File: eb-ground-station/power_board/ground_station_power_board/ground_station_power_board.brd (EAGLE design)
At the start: 142 x 81.8 mm, 52 parts, among them J1 CONN_20X2SHROUDED, U1 ADS1115IDGSTDGS10-M, U2 MCP23017T-E/SOSOIC28-W_MC-M, U3 MICROCHIP-TC427-MOSFET-DRIVER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, U4 MICROCHIP-TC427-MOSFET-DRIVER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, U5 MICROCHIP-TC427-MOSFET-DRIVER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, U6 NCV1117ST33T3G, U7 EXB-A10P391JC_ARRAY_EXBA-M, U8 EXB-A10P391JC_ARRAY_EXBA-M, U9 EXB-A10P391JC_ARRAY_EXBA-M

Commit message: Power board is mostly wrapped up
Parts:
- removed J2, J3: (no value), SparkFun-Connectors:1X03_LONGPADS
- removed R10, R11, R12, R4, R5, R6, R7, R8, R9: (no value), SparkFun-Resistors:0603
- removed U5: MICROCHIP-TC427-MOSFET-DRIVERSOIC8, GROUND-STATION-POWER-BOARD:SOIC8
- removed U6: NCV1117ST33T3G, NCV1117ST33T3G:SOT230P700X180-4N
- added D1, D10, D11, D12, D13, D14, D15, D16, D17, D2, D3, D4, D5, D6, D7, D8, D9: (no value), SparkFun-LED:LED-0603
- added J4: (no value), SparkFun-Connectors:1X06_LONGPADS
- added J5: (no value), SparkFun-Connectors:1X04_LONGPADS
- added U$19, U$20, U$21, U$25, U$26, U$27, U$28: RES-ARRAY-742C083, GROUND-STATION-POWER-BOARD:RES-ARRAY-742C083
- added U$22, U$23, U$24: TC4427-FET-GATE-DRVR, GROUND-STATION-POWER-BOARD:TSSOP-8
- R3: value 220 -> 800
- U$7: value 1714971-PHONEIX-CONTACT-TERMINAL-BLOCK -> 1714955-PHONEIX-CONTACT-TERMINAL-BLOCK; device GROUND-STATION-POWER-BOARD:1714971-PHONEIX-CONTACT-TERMINAL-BLOCK -> GROUND-STATION-POWER-BOARD:1714955-PHONEIX-CONTACT-TERMINAL-BLOCK
- U2: value MCP23017T-E/SOSOIC28-W_MC-M -> MCP23017T-E/SOQFN; device GROUND-STATION-POWER-BOARD:SOIC28-W_MC-M -> GROUND-STATION-POWER-BOARD:QFN28_6X6MC-M
- U3: value MICROCHIP-TC427-MOSFET-DRIVERSOIC8 -> MIC5239-3.3YMMMSOP-8_MM-M; device GROUND-STATION-POWER-BOARD:SOIC8 -> GROUND-STATION-POWER-BOARD:MSOP-8_MM-M
- U4: value MICROCHIP-TC427-MOSFET-DRIVERSOIC8 -> MCP9808T-E/MCDFN8_2X3MC-M; device GROUND-STATION-POWER-BOARD:SOIC8 -> GROUND-STATION-POWER-BOARD:DFN8_2X3MC-M
- moved R3 131.5 mm to (116.2, 27.4)
- moved U4 87.6 mm to (12.0, 70.0), turned to 0 degrees
- moved U$9 82.6 mm to (41.5, 25.2), turned to 0 degrees
- moved U9 81.5 mm to (60.6, 25.9), turned to 180 degrees
- moved C5 80.9 mm to (15.0, 34.5), turned to 180 degrees
- moved C7 75.6 mm to (31.1, 42.4), turned to 0 degrees
- moved C9 71.9 mm to (45.8, 36.7), turned to 270 degrees
- moved C6 70.5 mm to (30.9, 37.9), turned to 270 degrees
- moved R2 66.5 mm to (15.0, 38.5)
- moved C10 63.3 mm to (59.8, 36.7), turned to 270 degrees
- moved C8 60.5 mm to (52.8, 36.7), turned to 270 degrees
- moved R1 59.9 mm to (15.0, 36.5)
- moved U$17 59.1 mm to (48.5, 25.2)
- moved C3 56.3 mm to (32.8, 38.0), turned to 270 degrees
- moved C4 55.2 mm to (39.0, 38.0), turned to 270 degrees
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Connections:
- removed net N$10: R12.1
- removed net N$21: R11.2, U$8.2
- removed net N$23: R12.2, U$8.5
- removed net N$25: R6.2, U$17.2
- removed net N$30: R5.2, U$18.2
- removed net N$31: R8.2, U$15.5
- removed net N$32: R3.2, U$18.5
- removed net N$33: R9.2, U$9.2
- removed net N$34: R10.2, U$9.5
- removed net N$5: R7.1
- removed net N$6: R8.1
- removed net N$7: R9.1
- removed net N$8: R10.1
- new net ADC1: U$5.3, U1.7
- new net ADC2: U$5.1, U1.6
- new net ADC3: U$6.3, U1.5
- new net ADC4: U$6.1, U1.4
- new net G1: U$21.6, U$8.5
- new net G10: U$17.2, U$20.4
- new net G2: U$21.8, U$8.2
- new net G3: U$19.2, U$9.5
- new net G4: U$19.4, U$9.2
- new net G5: U$15.5, U$19.6
- new net G6: U$15.2, U$19.8
- new net G7: U$18.5, U$20.6
- new net G8: U$18.2, U$20.8
- new net G9: U$17.5, U$20.2
- new net HIGH_OUT_1: U$24.7, U$3.4
- new net HIGH_OUT_2: U$24.5, U$3.2
- new net HIGH_OUT_3: U$1.4, U$23.7
- new net HIGH_OUT_4: U$1.2, U$23.5
- new net HIGH_OUT_5: U$2.4, U$22.7
- new net HIGH_OUT_6: U$2.2, U$22.5
- new net LOW_OUT_1: U$18.3, U$4.3
- new net LOW_OUT_2: U$18.6, U$4.4
- new net LOW_OUT_3: U$17.3, U$4.2
- new net LOW_OUT_4: U$17.6, U$4.1
- new net N$14: D6.A, U$26.8
- new net N$15: D7.A, U$26.6
- new net N$16: D8.A, U$26.4
- new net N$17: D9.A, U$26.2
- new net N$27: D11.A, U$27.6
- new net N$28: D12.A, U$27.4
- new net N$38: D14.A, U$28.8
- new net N$39: D15.A, U$28.6
- new net N$40: D16.A, U$28.4
- new net N$41: D17.A, U$28.2
- new net RX: J4.4
- new net TX: J4.5
- net 12V: now also D5.A, U$22.6, U$23.6, U$24.6, U3.1, U3.3; no longer U3.6, U4.6, U5.6, U6.3
- net 3.3V: now also J4.3, J5.3, U2.5, U3.4, U4.8; no longer U2.9, U6.2, U6.4
- net GND: now also D1.C, D10.C, D11.C, D12.C, D13.C, D14.C, D15.C, D16.C, D17.C, D2.C, D3.C, D4.C, D6.C, D7.C, D8.C, D9.C, J4.1, J5.4, R3.2, U$22.3, U$23.3, U$24.3, U$5.2, U$5.4, U$6.2, U$6.4, U1.1, U2.11, U2.12, U2.13, U2.14, U2.29, U2.6, U3.5, U3.6, U3.7, U3.8, U4.4, U4.5, U4.6, U4.7, U4.9; no longer U2.10, U2.18, U3.3, U4.3, U5.3, U6.1
- net N$1: now also D1.A, U$25.8; no longer R3.1
- net N$2: now also D2.A, U$25.6; no longer R5.1
- net N$26: now also D10.A, U$27.8; no longer R4.2, U$17.5
- net N$29: now also D13.A, U$27.2; no longer R7.2, U$15.2
- net N$3: now also D3.A, U$25.4; no longer R4.1
- net N$4: now also D4.A, U$25.2; no longer R6.1
- net N$9: now also D5.C, R3.1; no longer R11.1
- net OUT1: now also U$24.4, U$26.5, U2.27, U8.2; no longer U2.21, U8.6
- net OUT10: now also U$20.1, U$27.5, U2.23; no longer U2.2
- net OUT11: now also U$19.3, U$28.7, U2.20, U7.8; no longer U2.3, U7.7
- net OUT12: now also U$19.7, U$27.3, U2.22, U7.7; no longer U2.4, U7.3
- net OUT13: now also U$19.5, U$27.1, U2.21, U7.3; no longer U2.5, U7.8
- net OUT14: now also U$19.1, U$28.5, U2.19; no longer U2.6
- net OUT15: now also U$21.7, U$28.3, U2.18; no longer U2.7
- net OUT16: now also U$21.5, U$28.1, U2.17; no longer U2.8
- net OUT2: now also U$24.2, U$26.7, U2.28, U8.8; no longer U2.22, U8.4
- net OUT3: now also U$23.4, U$25.5, U2.3, U8.4; no longer U2.23, U8.7
- net OUT4: now also U$23.2, U$25.7, U2.4, U8.6; no longer U2.24, U8.3
- net OUT5: now also U$22.4, U$25.1, U2.1, U8.3; no longer U2.25, U8.8
- net OUT6: now also U$22.2, U$25.3, U2.2, U8.7; no longer U2.26, U8.2
- net OUT7: now also U$20.7, U$26.3, U2.26; no longer U2.27
- net OUT8: now also U$20.5, U$26.1, U2.25; no longer U2.28
- net OUT9: now also U$20.3, U$27.7, U2.24; no longer U2.1
- net PWR_FET_G1: now also U$10.G, U9.8; no longer U$16.G, U9.1
- net PWR_FET_G2: now also U$16.G, U9.2; no longer U$10.G, U9.9
- net PWR_FET_G3: now also U$12.G, U9.7; no longer U$11.G, U9.2
- net PWR_FET_G4: now also U$11.G, U9.3; no longer U$12.G, U9.8
- net PWR_FET_G5: now also U$14.G, U9.6; no longer U$13.G, U9.3
- net PWR_FET_G6: now also U$13.G, U9.4; no longer U$14.G, U9.7
- net SCL: now also J5.1, U2.8, U4.2; no longer U2.12
- net SDA: now also J5.2, U2.9, U4.1; no longer U2.13
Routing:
- net PWR_FET_G2: track 0.00 -> 81.1 mm, vias 0 -> 2
- net N$40: track 0.00 -> 75.3 mm
- net SDA: track 0.00 -> 73.6 mm, vias 0 -> 3
- net N$15: track 0.00 -> 70.6 mm
- net N$41: track 0.00 -> 69.4 mm
- net SCL: track 0.00 -> 68.8 mm
- net PWR_FET_G1: track 0.00 -> 68.5 mm, vias 0 -> 2
- net 3.3V: track 0.00 -> 68.0 mm
- net HIGH_OUT_1: track 0.00 -> 67.9 mm, vias 0 -> 1
- net OUT1: track 0.00 -> 67.0 mm, vias 0 -> 2
- net N$14: track 0.00 -> 65.6 mm
- net N$38: track 0.00 -> 65.3 mm
- net HIGH_OUT_2: track 0.00 -> 65.1 mm, vias 0 -> 1
- net PWR_FET_G4: track 0.00 -> 64.5 mm, vias 0 -> 2
- net OUT2: track 0.00 -> 64.1 mm, vias 0 -> 2
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- added copper zone on layer 1, net 12V
- added copper zone on layer 16, net 12V
- added copper zone on layer 1, net GND
- added copper zone on layer 16, net GND
- added copper zone on layer 1, net PWR_P_FET_1
- added copper zone on layer 1, net PWR_P_FET_2
- added copper zone on layer 1, net PWR_P_FET_3
- added copper zone on layer 1, net PWR_P_FET_4
- added copper zone on layer 1, net PWR_P_FET_5
- added copper zone on layer 1, net PWR_P_FET_6
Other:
- board size 142 x 81.8 mm -> 125 x 78 mm
- board text added: "1"
- board text added: "12V"
- board text added: "2"
- board text added: "3"
- board text added: "4"
- board text added: "5"
- board text added: "6"
- board text added: "A0"
- board text added: "A1"
- board text added: "A2"
- board text added: "A3"
- board text added: "A4"
- board text added: "A5"
- board text added: "A6"
- board text added: "A7"
- board text added: "ADC-IN"
- board text added: "B0"
- board text added: "B1"
- board text added: "B2"
- board text added: "B3"
- board text added: "B4"
- board text added: "B5"
- board text added: "B6"
- board text added: "B7"
- board text added: "G"
- board text added: "GND"
- board text added: "GROUND"
- board text added: "HIGH-SIDE"
- board text added: "HIGH-SIDE-HIGH-POWER"
- board text added: "LOW-SIDE"

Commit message: some final changes
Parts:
- removed U$10, U$11, U$12, U$13, U$14, U$16: SQJ459EP_MOSFET_P_CHAN, GROUND-STATION-POWER-BOARD:POWERPAK_S0-8L
- removed U$15, U$17, U$18, U$8, U$9: DMN61D8LVT-DUAL-N-CHANNEL-MOSFET, GROUND-STATION-POWER-BOARD:TSOT26
- removed U$19, U$20, U$21, U$25, U$26, U$27, U$28: RES-ARRAY-742C083, GROUND-STATION-POWER-BOARD:RES-ARRAY-742C083
- removed U$22, U$23, U$24: TC4427-FET-GATE-DRVR, GROUND-STATION-POWER-BOARD:TSSOP-8
- removed U7, U8, U9: EXB-A10P391JC_ARRAY_EXBA-M, temp-lib:C_ARRAY_EXBA-M
- added E1, E2: (no value), oresat-rcl:.0805-B
- added Q1, Q2, Q3, Q4, Q5, Q6: SQJ459EP_MOSFET_P_CHAN, GROUND-STATION-POWER-BOARD:POWERPAK_S0-8L
- added Q15, Q17, Q18, Q8, Q9: DMN61D8LVT-DUAL-N-CHANNEL-MOSFET, GROUND-STATION-POWER-BOARD:TSOT26
- added Q22, Q23, Q24: TC4427-FET-GATE-DRVR, GROUND-STATION-POWER-BOARD:TSSOP-8
- added R10, R8, R9: EXB-A10P391JC_ARRAY_EXBA-M, temp-lib:C_ARRAY_EXBA-M
- added R11, R12, R13: 220, GROUND-STATION-POWER-BOARD:RES-ARRAY-742C083
- added R4, R5, R6, R7: 680, GROUND-STATION-POWER-BOARD:RES-ARRAY-742C083
- C10, C4, C8, C9: device SparkFun-Capacitors:1206 -> SparkFun-Capacitors:0805
- C2: value 100UF-CAP-EMVH630ARA101MKE0SCHEMI-KE0-M -> 100UF
- C3: value 4.7uF -> 10uF; device SparkFun-Capacitors:1206 -> SparkFun-Capacitors:0805
- R3: value 800 -> 806
- moved U4 118.5 mm to (113.0, 8.00), turned to 180 degrees
- moved J4 115.8 mm to (112.0, 69.0), turned to 270 degrees
- moved J1 115.0 mm to (120.0, 39.0), turned to 180 degrees
- moved U$7 110.2 mm to (16.3, 8.97), turned to 0 degrees
- moved D5 106.7 mm to (15.9, 62.1), turned to 0 degrees
- moved R3 105.5 mm to (15.9, 60.0), turned to 180 degrees
- moved D16 99.6 mm to (26.5, 68.0), turned to 180 degrees
- moved J5 99.4 mm to (102.5, 61.4)
- moved C2 98.7 mm to (15.8, 23.2), turned to 0 degrees
- moved C5 95.4 mm to (110.0, 43.5), turned to 0 degrees
- moved R1 95.1 mm to (110.0, 41.5), turned to 180 degrees
- moved R2 95.0 mm to (110.0, 39.5), turned to 180 degrees
- moved U2 93.6 mm to (108.3, 48.4), turned to 90 degrees
- moved C1 93.0 mm to (16.6, 31.5), turned to 0 degrees
- moved D17 91.7 mm to (31.5, 68.0), turned to 180 degrees
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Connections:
- removed net RX: J4.4
- removed net TX: J4.5
- new net AGND: C6.2, E2.2, U$5.2, U$5.4, U$6.2, U$6.4, U1.1, U1.2, U1.3
- new net N$5: C6.1, E1.1, U1.8
- net 12V: now also Q1.S1, Q1.S2, Q1.S3, Q2.S1, Q2.S2, Q2.S3, Q22.6, Q23.6, Q24.6, Q3.S1, Q3.S2, Q3.S3, Q4.S1, Q4.S2, Q4.S3, Q5.S1, Q5.S2, Q5.S3, Q6.S1, Q6.S2, Q6.S3, R10.10, R10.5; no longer U$10.S1, U$10.S2, U$10.S3, U$11.S1, U$11.S2, U$11.S3, U$12.S1, U$12.S2, U$12.S3, U$13.S1, U$13.S2, U$13.S3, U$14.S1, U$14.S2, U$14.S3, U$16.S1, U$16.S2, U$16.S3, U$22.6, U$23.6, U$24.6, U9.10, U9.5
- net 3.3V: now also E1.2; no longer C6.1, U1.8
- net G1: now also Q8.5, R11.6; no longer U$21.6, U$8.5
- net G10: now also Q17.2, R13.4; no longer U$17.2, U$20.4
- net G2: now also Q8.2, R11.8; no longer U$21.8, U$8.2
- net G3: now also Q9.5, R12.2; no longer U$19.2, U$9.5
- net G4: now also Q9.2, R12.4; no longer U$19.4, U$9.2
- net G5: now also Q15.5, R12.6; no longer U$15.5, U$19.6
- net G6: now also Q15.2, R12.8; no longer U$15.2, U$19.8
- net G7: now also Q18.5, R13.6; no longer U$18.5, U$20.6
- net G8: now also Q18.2, R13.8; no longer U$18.2, U$20.8
- net G9: now also Q17.5, R13.2; no longer U$17.5, U$20.2
- net GND: now also E2.1, Q15.1, Q15.4, Q17.1, Q17.4, Q18.1, Q18.4, Q22.3, Q23.3, Q24.3, Q8.1, Q8.4, Q9.1, Q9.4, R8.10, R8.5, R9.10, R9.5; no longer C6.2, U$15.1, U$15.4, U$17.1, U$17.4, U$18.1, U$18.4, U$22.3, U$23.3, U$24.3, U$5.2, U$5.4, U$6.2, U$6.4, U$8.1, U$8.4, U$9.1, U$9.4, U1.1, U1.3, U7.10, U7.5, U8.10, U8.5
- net HIGH_OUT_1: now also Q24.7; no longer U$24.7
- net HIGH_OUT_2: now also Q24.5; no longer U$24.5
- net HIGH_OUT_3: now also Q23.7; no longer U$23.7
- net HIGH_OUT_4: now also Q23.5; no longer U$23.5
- net HIGH_OUT_5: now also Q22.7; no longer U$22.7
- net HIGH_OUT_6: now also Q22.5; no longer U$22.5
- net LOW_OUT_1: now also Q18.3; no longer U$18.3
- net LOW_OUT_2: now also Q18.6; no longer U$18.6
- net LOW_OUT_3: now also Q17.3; no longer U$17.3
- net LOW_OUT_4: now also Q17.6; no longer U$17.6
- net N$1: now also R4.8; no longer U$25.8
- net N$14: now also R5.8; no longer U$26.8
- net N$15: now also R5.6; no longer U$26.6
- net N$16: now also R5.4; no longer U$26.4
- net N$17: now also R5.2; no longer U$26.2
- net N$2: now also R4.6; no longer U$25.6
- net N$26: now also R6.8; no longer U$27.8
- net N$27: now also R6.6; no longer U$27.6
- net N$28: now also R6.4; no longer U$27.4
- net N$29: now also R6.2; no longer U$27.2
- net N$3: now also R4.4; no longer U$25.4
- net N$38: now also R7.8; no longer U$28.8
- net N$39: now also R7.6; no longer U$28.6
- net N$4: now also R4.2; no longer U$25.2
- net N$40: now also R7.4; no longer U$28.4
- net N$41: now also R7.2; no longer U$28.2
- net OUT1: now also Q24.4, R5.5, R8.2; no longer U$24.4, U$26.5, U8.2
- net OUT10: now also R13.1, R6.5, R9.4; no longer U$20.1, U$27.5, U7.4
- net OUT11: now also R12.3, R7.7, R9.8; no longer U$19.3, U$28.7, U7.8
- net OUT12: now also R12.7, R6.3, R9.7; no longer U$19.7, U$27.3, U7.7
- net OUT13: now also R12.5, R6.1, R9.3; no longer U$19.5, U$27.1, U7.3
- net OUT14: now also R12.1, R7.5, R9.2; no longer U$19.1, U$28.5, U7.2
- net OUT15: now also R11.7, R7.3, R9.9; no longer U$21.7, U$28.3, U7.9
- net OUT16: now also R11.5, R7.1, R9.1; no longer U$21.5, U$28.1, U7.1
- net OUT2: now also Q24.2, R5.7, R8.8; no longer U$24.2, U$26.7, U8.8
- net OUT3: now also Q23.4, R4.5, R8.4; no longer U$23.4, U$25.5, U8.4
- net OUT4: now also Q23.2, R4.7, R8.6; no longer U$23.2, U$25.7, U8.6
- net OUT5: now also Q22.4, R4.1, R8.3; no longer U$22.4, U$25.1, U8.3
- net OUT6: now also Q22.2, R4.3, R8.7; no longer U$22.2, U$25.3, U8.7
- net OUT7: now also R13.7, R5.3, R8.9; no longer U$20.7, U$26.3, U8.9
- net OUT8: now also R13.5, R5.1, R8.1; no longer U$20.5, U$26.1, U8.1
- net OUT9: now also R13.3, R6.7, R9.6; no longer U$20.3, U$27.7, U7.6
- net PWR_FET_G1: now also Q2.G, Q8.3, R10.8; no longer U$10.G, U$8.3, U9.8
- net PWR_FET_G2: now also Q1.G, Q8.6, R10.2; no longer U$16.G, U$8.6, U9.2
- net PWR_FET_G3: now also Q4.G, Q9.3, R10.7; no longer U$12.G, U$9.3, U9.7
- net PWR_FET_G4: now also Q3.G, Q9.6, R10.3; no longer U$11.G, U$9.6, U9.3
- net PWR_FET_G5: now also Q15.3, Q6.G, R10.6; no longer U$14.G, U$15.3, U9.6
- net PWR_FET_G6: now also Q15.6, Q5.G, R10.4; no longer U$13.G, U$15.6, U9.4
- net PWR_P_FET_1: now also Q6.D1; no longer U$14.D1
- net PWR_P_FET_2: now also Q5.D1; no longer U$13.D1
- net PWR_P_FET_3: now also Q4.D1; no longer U$12.D1
- net PWR_P_FET_4: now also Q3.D1; no longer U$11.D1
- net PWR_P_FET_5: now also Q2.D1; no longer U$10.D1
- net PWR_P_FET_6: now also Q1.D1; no longer U$16.D1
- net RX_UART: now also J4.4
- net TX_UART: now also J4.5
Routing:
- net TX_UART: track 0.00 -> 40.2 mm
- net RX_UART: track 0.00 -> 40.2 mm
- net 3.3V: track 68.0 -> 106.5 mm, vias 0 -> 4
- net SDA: track 73.6 -> 103.4 mm
- net SCL: track 68.8 -> 95.7 mm, vias 0 -> 2
- net 12V: track 46.8 -> 55.8 mm
- net N$38: track 65.3 -> 56.5 mm
- net N$29: track 49.6 -> 40.8 mm
- net N$1: track 46.6 -> 37.8 mm
- net N$4: track 60.6 -> 51.8 mm
- net N$3: track 55.7 -> 46.9 mm
- net N$26: track 43.7 -> 34.9 mm
- net N$17: track 38.4 -> 29.6 mm
- net N$41: track 69.4 -> 60.6 mm
- net N$40: track 75.3 -> 66.5 mm
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- added copper zone on layer 1, net AGND
- added copper zone on layer 16, net AGND
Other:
- outline, holes or cut-outs redrawn
- board text added: "3.3V"
- board text added: "I2C"
- board text added: "I2C ADDRS: ADC : 0x48 GPIO : 0x20 TEMP : 0x18"
- board text added: "ORESAT GROUND STATION POWER BOARD OLIVER REW 2018-07-29"
- board text added: "RX"
- board text added: "SCL"
- board text added: "SDA"
- board text added: "TX"
- board text added: "UART"

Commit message: Approved ERC and DRC
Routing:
- net GND: vias 286 -> 289
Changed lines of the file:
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@@
 <via x="108" y="48" extent="1-16" drill="0.254"/>
 <via x="87.5" y="69" extent="1-16" drill="0.254"/>
+<via x="110" y="52.75" extent="1-16" drill="0.254"/>
+<via x="111.125" y="52" extent="1-16" drill="0.254"/>
+<via x="106.5" y="55" extent="1-16" drill="0.254"/>
 </signal>
 <signal name="OUT16">
@@
 <wire x1="49.75" y1="47.25" x2="49.75" y2="43" width="0.2" layer="16"/>
 <via x="49.75" y="43" extent="1-16" drill="0.254"/>
-<wire x1="49.7925" y1="43.0425" x2="49.75" y2="43" width="0.2" layer="1"/>
 <contactref element="Q15" pad="6"/>
 <wire x1="81.5874" y1="54.49655" x2="81.43955" y2="54.6444" width="0.2" layer="1"/>
@@
 <wire x1="64.04" y1="50.170625" x2="63.405625" y2="50.805" width="0.2" layer="1"/>
 <wire x1="63.405625" y1="50.805" x2="62.7827" y2="50.805" width="0.2" layer="1"/>
-<wire x1="49.83" y1="43.005" x2="49.7925" y2="43.0425" width="0.2" layer="1"/>
 <contactref element="Q5" pad="G"/>
 <wire x1="49.75" y1="43" x2="49.755" y2="43.005" width="0.2" layer="1"/>
@@
 <mfgpreviewcolor name="substratecolor" color="0xFF786E46"/>
 </mfgpreviewcolors>
+<errors>
+</errors>
 </board>
 </drawing>

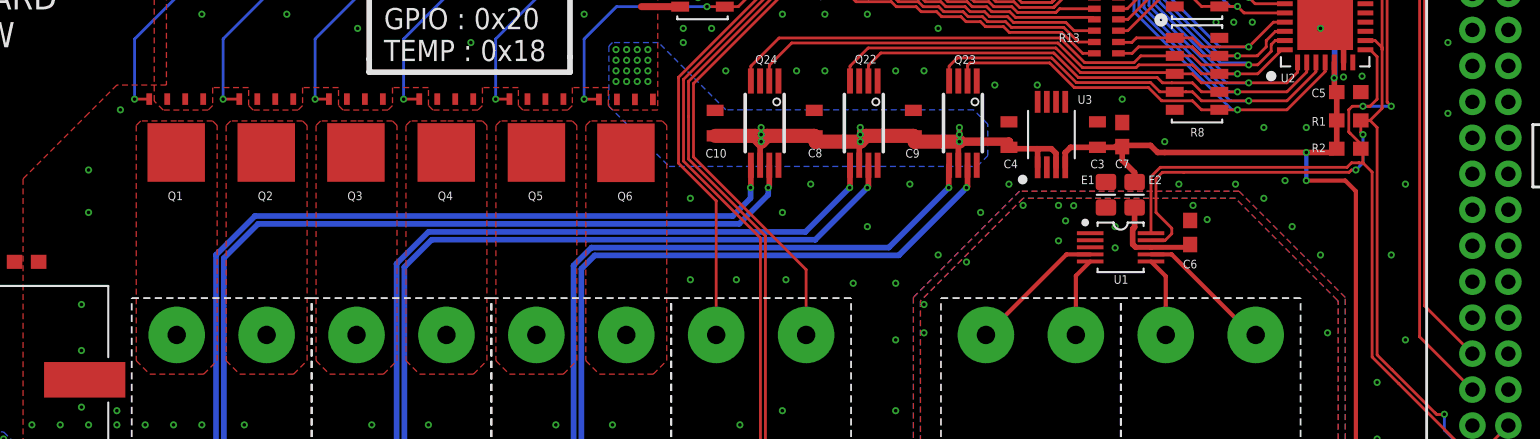
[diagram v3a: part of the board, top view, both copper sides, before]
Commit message: added vias
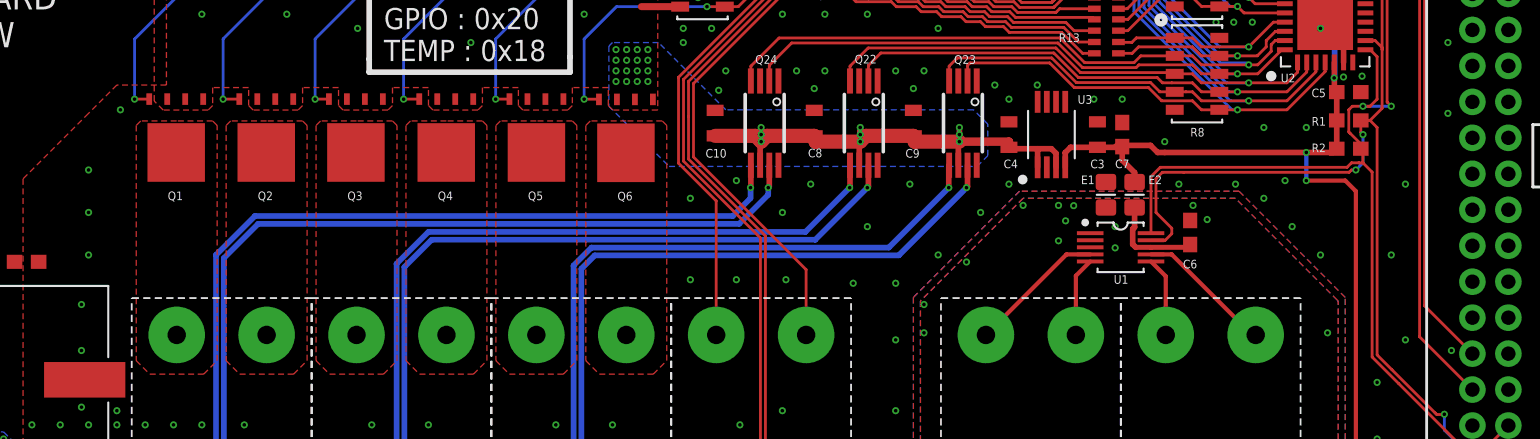
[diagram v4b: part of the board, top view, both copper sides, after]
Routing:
- net GND: vias 289 -> 297
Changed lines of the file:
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@@
 <via x="111.125" y="52" extent="1-16" drill="0.254"/>
 <via x="106.5" y="55" extent="1-16" drill="0.254"/>
+<via x="21" y="32" extent="1-16" drill="0.254"/>
+<via x="92" y="43" extent="1-16" drill="0.254"/>
+<via x="86" y="43" extent="1-16" drill="0.254"/>
+<via x="79.25" y="43.75" extent="1-16" drill="0.254"/>
+<via x="72.25" y="43.75" extent="1-16" drill="0.254"/>
+<via x="65.5" y="43.625" extent="1-16" drill="0.254"/>
+<via x="66.75" y="37.25" extent="1-16" drill="0.254"/>
+<via x="117.25" y="25.25" extent="1-16" drill="0.254"/>
 </signal>
 <signal name="OUT16">
